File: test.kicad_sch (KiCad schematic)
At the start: 1 part, among them U1 STM32F401C_D-E_Ux

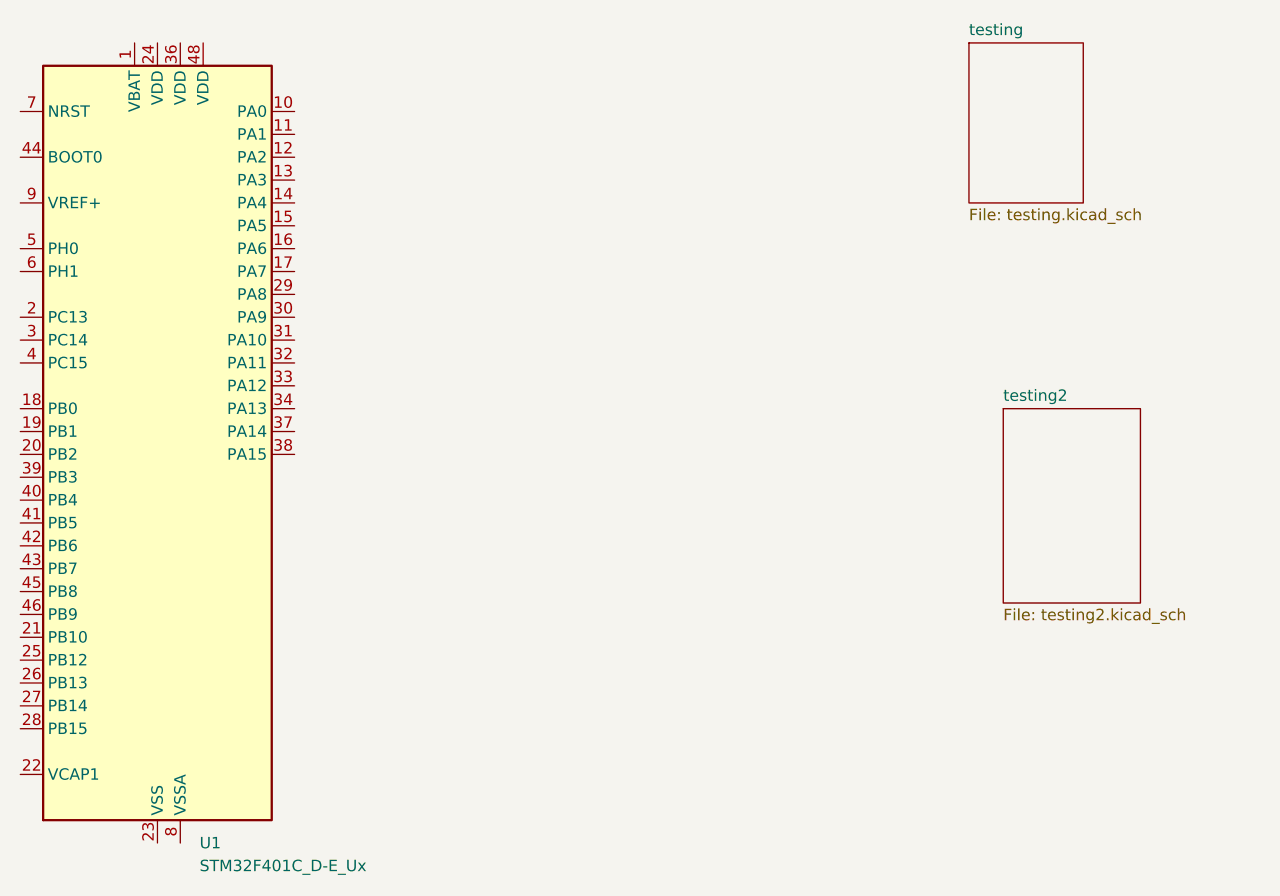
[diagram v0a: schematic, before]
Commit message: added OSC
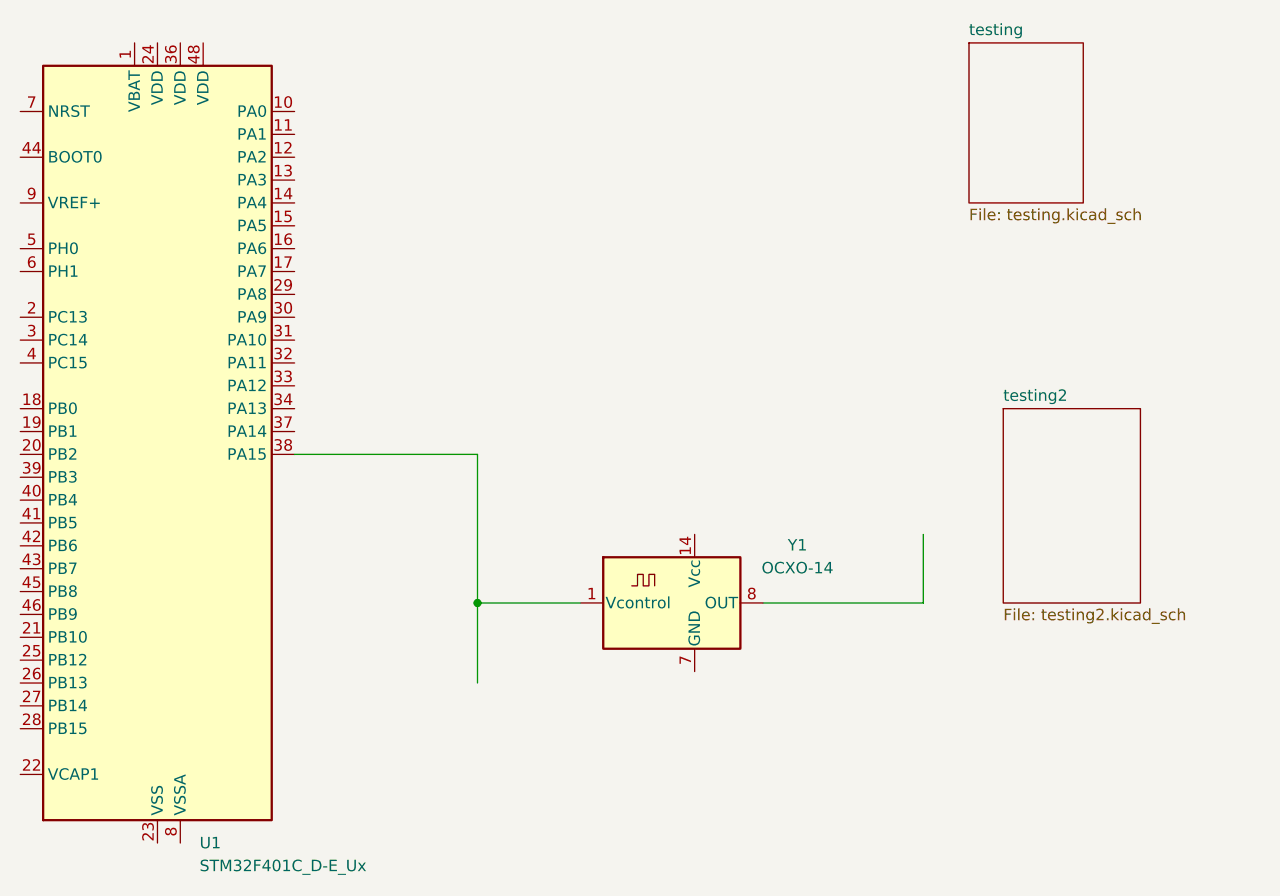
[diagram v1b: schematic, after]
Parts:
- added Y1: OCXO-14, Oscillator:Oscillator_DIP-14, symbol Oscillator:OCXO-14
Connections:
- net at U1.38 (PA15): now also Y1.1 (Vcontrol)
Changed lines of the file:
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@@
 		(company "jdpcb")
+	)
+	(junction
+		(at 171.45 111.76)
+		(diameter 0)
+		(color 0 0 0 0)
+	)
+	(wire
+		(pts
+			(xy 203.2 111.76) (xy 220.98 111.76)
+		)
+		(stroke
+			(width 0)
+			(type default)
+		)
+	)
+	(wire
+		(pts
+			(xy 220.98 104.14) (xy 220.98 111.76)
+		)
+		(stroke
+			(width 0)
+			(type default)
+		)
+	)
+	(wire
+		(pts
+			(xy 171.45 111.76) (xy 171.45 120.65)
+		)
+		(stroke
+			(width 0)
+			(type default)
+		)
+	)
+	(wire
+		(pts
+			(xy 171.45 111.76) (xy 182.88 111.76)
+		)
+		(stroke
+			(width 0)
+			(type default)
+		)
+	)
+	(wire
+		(pts
+			(xy 151.13 95.25) (xy 171.45 95.25)
+		)
+		(stroke
+			(width 0)
+			(type default)
+		)
+	)
+	(wire
+		(pts
+			(xy 171.45 95.25) (xy 171.45 111.76)
+		)
+		(stroke
+			(width 0)
+			(type default)
+		)
 	)
 	(symbol
@@
 					(unit 1)
 				)
+			)
+		)
+	)
+	(symbol
+		(lib_id "Oscillator:OCXO-14")
+		(at 195.58 111.76 0)
+		(unit 1)
+		(exclude_from_sim no)
+		(in_bom yes)
+		(on_board yes)
+		(dnp no)
+		(fields_autoplaced yes)
+		(property "Reference" "Y1"
+			(at 207.01 105.3398 0)
+			(effects
+				(font
+					(size 1.27 1.27)
+				)
+			)
+		)
+		(property "Value" "OCXO-14"
+			(at 207.01 107.8798 0)
+			(effects
+				(font
+					(size 1.27 1.27)
+				)
+			)
+		)
+		(property "Footprint" "Oscillator:Oscillator_DIP-14"
+			(at 207.01 120.65 0)
+			(effects
+				(font
+					(size 1.27 1.27)
+				)
+				(hide yes)
+			)
+		)
+		(property "Datasheet" "http://www.petermann-technik.de/fileadmin/petermann/pdf/crystal-oscillators/OCXO-14_PETERMANN-TECHNIK.pdf"
+			(at 187.96 109.22 0)
+			(effects
+				(font
+					(size 1.27 1.27)
+				)
+				(hide yes)
+			)
+		)
+		(property "Description" "Voltage-Controlled Crystal Clock Oscillator, DIP14-style metal package"
+			(at 195.58 111.76 0)
+			(effects
+				(font
+					(size 1.27 1.27)
+				)
+				(hide yes)
+			)
+		)
+		(pin "1"
+		)
+		(pin "14"
+		)
+		(pin "7"
+		)
+		(pin "8"
+		)
+		(instances
+			(project ""
+				(path "/979d9f90-9363-4450-94d2-ffc714d47830"
+					(reference "Y1")
+					(unit 1)
+				)

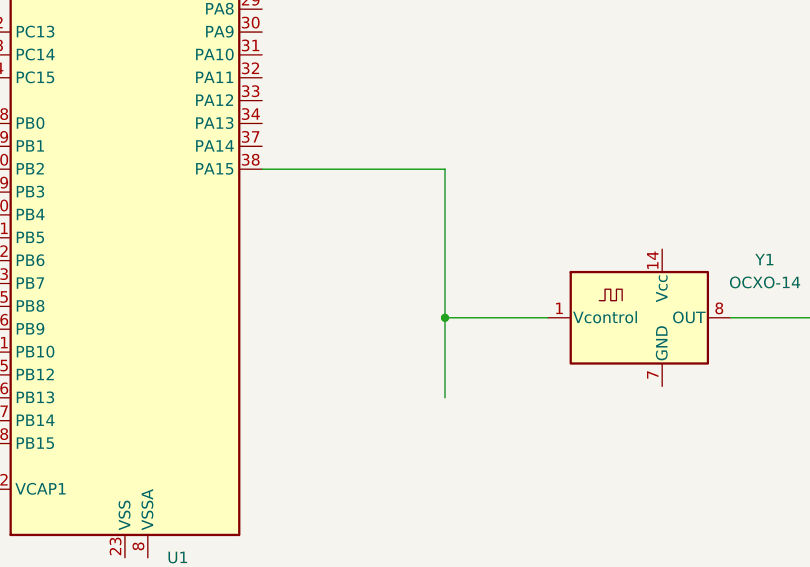
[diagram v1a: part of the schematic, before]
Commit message: removed connection
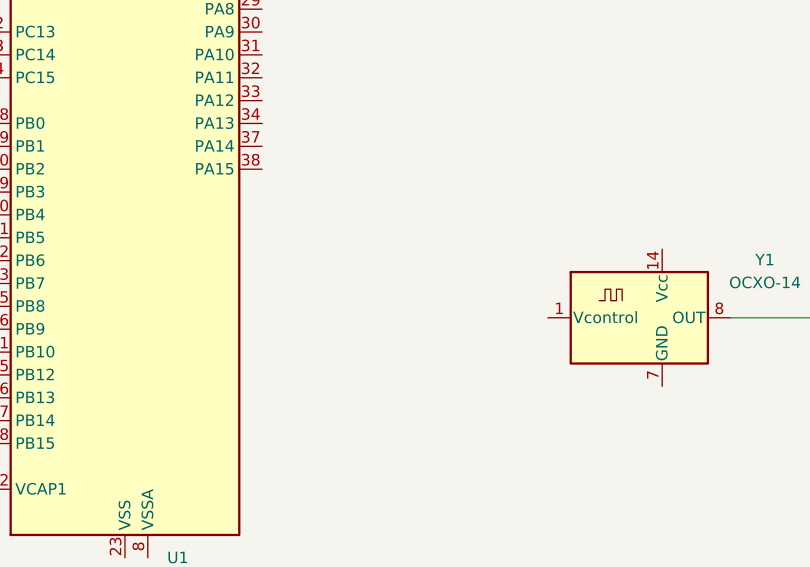
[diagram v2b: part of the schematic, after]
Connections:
- net at U1.38 (PA15): no longer Y1.1 (Vcontrol)
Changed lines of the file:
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@@
 		(company "jdpcb")
-	)
-	(junction
-		(at 171.45 111.76)
-		(diameter 0)
-		(color 0 0 0 0)
 	)
 	(wire
@@
 		)
 		(stroke
-			(width 0)
-			(type default)
-		)
-	)
-	(wire
-		(pts
-			(xy 171.45 111.76) (xy 171.45 120.65)
-		)
-		(stroke
-			(width 0)
-			(type default)
-		)
-	)
-	(wire
-		(pts
-			(xy 171.45 111.76) (xy 182.88 111.76)
-		)
-		(stroke
-			(width 0)
-			(type default)
-		)
-	)
-	(wire
-		(pts
-			(xy 151.13 95.25) (xy 171.45 95.25)
-		)
-		(stroke
-			(width 0)
-			(type default)
-		)
-	)
-	(wire
-		(pts
-			(xy 171.45 95.25) (xy 171.45 111.76)
-		)
-		(stroke
